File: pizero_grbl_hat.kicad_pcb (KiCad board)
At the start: 2 copper layers, 65 x 30 mm, 31 parts, among them J1 GPIO_CONNECTOR, J2 ISP, J3 LIMIT_X, J4 LIMIT_Y, J5 VMOT, J6 MOTOR_X, J7 MOTOR_Y, U1 ATmega328P-AU, Y1 16MHz

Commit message: finish layout and print schematics
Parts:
- removed A1: X-axis, Module:Pololu_Breakout-16_15.2x20.3mm
- removed C3, C7: 100n, Capacitor_SMD:C_0805_2012Metric
- removed C6: 10u, Capacitor_SMD:C_0805_2012Metric
- removed TP1, TP2, TP3, TP4, TP5, TP6: TestPoint_2Pole, TestPoint:TestPoint_2Pads_Pitch2.54mm_Drill0.8mm
- added C9: 100u, Capacitor_SMD:CP_Elec_6.3x7.7, F.Cu at (153.3, 106.0)
- added I2C: I2C, Connector_JST:JST_PH_B4B-PH-K_1x04_P2.00mm_Vertical, F.Cu at (121.0, 103.0)
- added X-Axis: X-axis, Module:Pololu_Breakout-16_15.2x20.3mm, F.Cu at (140.1, 112.3)
- C1: footprint Capacitor_SMD:C_0805_2012Metric -> Capacitor_SMD:C_0805_2012Metric_Pad1.15x1.40mm_HandSolder; moved to F.Cu
- R1: footprint Resistor_SMD:R_0805_2012Metric -> Resistor_SMD:R_0805_2012Metric_Pad1.15x1.40mm_HandSolder
- Y1: footprint Crystal:Crystal_SMD_2012-2Pin_2.0x1.2mm -> Crystal:Crystal_SMD_Abracon_ABM3-2Pin_5.0x3.2mm_HandSoldering
- moved C2 23.5 mm to (128.6, 98.6)
- moved R2 23.3 mm to (125.0, 98.6)
- moved C8 9.66 mm to (175.9, 105.7), turned to 180 degrees
- moved C1 7.14 mm to (125.1, 107.8), turned to 270 degrees
- moved R1 5.07 mm to (129.7, 108.5), turned to 0 degrees
- moved J2 4.02 mm to (142.6, 103.5), turned to 0 degrees
- moved Y1 2.79 mm to (132.0, 105.2), turned to 0 degrees
- moved C4 2.13 mm to (136.3, 105.2), turned to 270 degrees
- moved U1 1.55 mm to (129.5, 105.2)
- moved C5 1.07 mm to (136.3, 108.8), turned to 270 degrees
- renumbered J3 to Limit-X, J4 to Limit-Y, J6 to Motor-X, J7 to Motor-Y, J5 to VSTEP, A2 to Y-Axis
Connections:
- J1 pad 3: /GPIO2_SDA1 -> SDA
- J1 pad 5: /GPIO3_SCL1 -> SCL
- Y-Axis pad 10: Net-(A2-Pad10) -> +3V3
- Y-Axis pad 11: Net-(A2-Pad11) -> +3V3
- Y-Axis pad 12: Net-(A2-Pad12) -> +3V3
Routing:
- net +3V3: track 142.0 -> 110.7 mm, vias 0 -> 2
- net SCL: track 0.00 -> 15.5 mm
- net SDA: track 0.00 -> 12.4 mm
- net RESET: track 38.9 -> 28.0 mm
- net GND: track 72.2 -> 80.2 mm, vias 7 -> 1
- net Net-(A2-Pad12): track 5.08 -> 0.00 mm
- net Net-(A2-Pad11): track 5.08 -> 0.00 mm
- net Net-(A2-Pad10): track 5.08 -> 0.00 mm
- net Net-(A1-Pad12): track 5.08 -> 0.00 mm
- net Net-(A1-Pad11): track 5.08 -> 0.00 mm
- net Net-(A1-Pad10): track 5.08 -> 0.00 mm
- net MOSI: track 26.1 -> 22.4 mm, vias 2 -> 0
- net STEPX: track 15.2 -> 11.8 mm, vias 1 -> 0
- net DIRX: track 20.9 -> 17.5 mm
- net Net-(A1-Pad8): track 47.0 -> 44.0 mm
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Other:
- board text added: "GRBL-Hat rev0"
- board text added: "daniel@tydirium.org"
- board text removed: "GRBL Hat rev0 (c) 2019 Daniel Winters daniel@tydirium.org"

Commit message: start working on rev1, work in progress
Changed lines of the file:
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@@
-(kicad_pcb (version 20171130) (host pcbnew "(5.1.4-0-10_14)")
+(kicad_pcb (version 20171130) (host pcbnew "(5.1.5-0-10_14)")
   (general
     (thickness 1.6)
@@
   )
   (layers
-    (0 F.Cu signal)
+    (0 F.Cu signal hide)
     (31 B.Cu signal)
-    (32 B.Adhes user)
-    (33 F.Adhes user)
+    (32 B.Adhes user hide)
+    (33 F.Adhes user hide)
     (34 B.Paste user)
-    (35 F.Paste user)
+    (35 F.Paste user hide)
     (36 B.SilkS user)
-    (37 F.SilkS user)
+    (37 F.SilkS user hide)
     (38 B.Mask user)
     (39 F.Mask user)
@@
     (descr "Pololu Breakout 16-pin 15.2x20.3mm 0.6x0.8\\")
     (tags "Pololu Breakout")
-    (fp_text reference X-Axis (at 6.35 -2.54 90) (layer F.SilkS)
+    (fp_text reference X-Axis (at 6.35 -2.032 90) (layer F.SilkS)
       (effects (font (size 1 1) (thickness 0.15)))
     )
@@
     (descr "Through hole straight socket strip, 2x20, 2.54mm pitch, double cols (from Kicad 4.0.7), script generated")
     (tags "Through hole socket strip THT 2x20 2.54mm double row")
-    (fp_text reference J1 (at 2.8 -16.3) (layer B.SilkS)
+    (fp_text reference J1 (at 1.778 -20.53) (layer B.SilkS)
       (effects (font (size 1 1) (thickness 0.15)) (justify mirror))
     )
@@
     (tags capacitor)
     (attr smd)
-    (fp_text reference C2 (at 0 1.65) (layer B.SilkS)
+    (fp_text reference C2 (at -2.8725 0.508) (layer B.SilkS)
       (effects (font (size 1 1) (thickness 0.15)) (justify mirror))
     )
@@
     (tags capacitor)
     (attr smd)
-    (fp_text reference C4 (at 0 1.65 90) (layer B.SilkS)
+    (fp_text reference C4 (at -0.1755 -1.778 90) (layer B.SilkS)
       (effects (font (size 1 1) (thickness 0.15)) (justify mirror))
     )
@@
     (tags capacitor)
     (attr smd)
-    (fp_text reference C5 (at 0 1.65 270) (layer B.SilkS)
+    (fp_text reference C5 (at -0.508 -1.778 270) (layer B.SilkS)
       (effects (font (size 1 1) (thickness 0.15)) (justify mirror))
     )
@@
     (tags "QFP 0.8")
     (attr smd)
-    (fp_text reference U1 (at 0 6.05 180) (layer B.SilkS)
+    (fp_text reference U1 (at -4.699 5.061 180) (layer B.SilkS)
       (effects (font (size 1 1) (thickness 0.15)) (justify mirror))
     )
@@
     (tags "resistor handsolder")
     (attr smd)
-    (fp_text reference R1 (at 0 1.524) (layer F.SilkS)
+    (fp_text reference R1 (at 0 2.032) (layer F.SilkS)
       (effects (font (size 1 1) (thickness 0.15)))
     )
@@
     )
   )
-  (gr_text daniel@tydirium.org (at 130.938 101.172) (layer F.SilkS)
+  (gr_text daniel@tydirium.org (at 131.192 100.664) (layer F.SilkS)
     (effects (font (size 1 1) (thickness 0.15)))
   )
-  (gr_text "GRBL-Hat rev0" (at 129.668 98.378) (layer F.SilkS)
+  (gr_text "GRBL-Hat rev0" (at 129.414 99.14) (layer F.SilkS)
     (effects (font (size 1 1) (thickness 0.15)))
   )

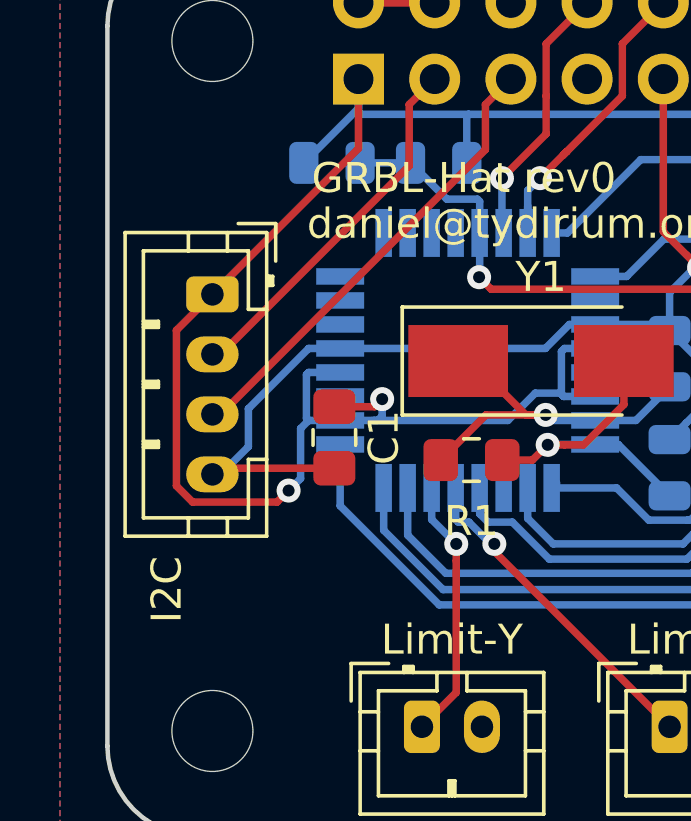
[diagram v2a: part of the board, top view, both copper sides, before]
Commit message: show I2C pins on front and back silkscreen
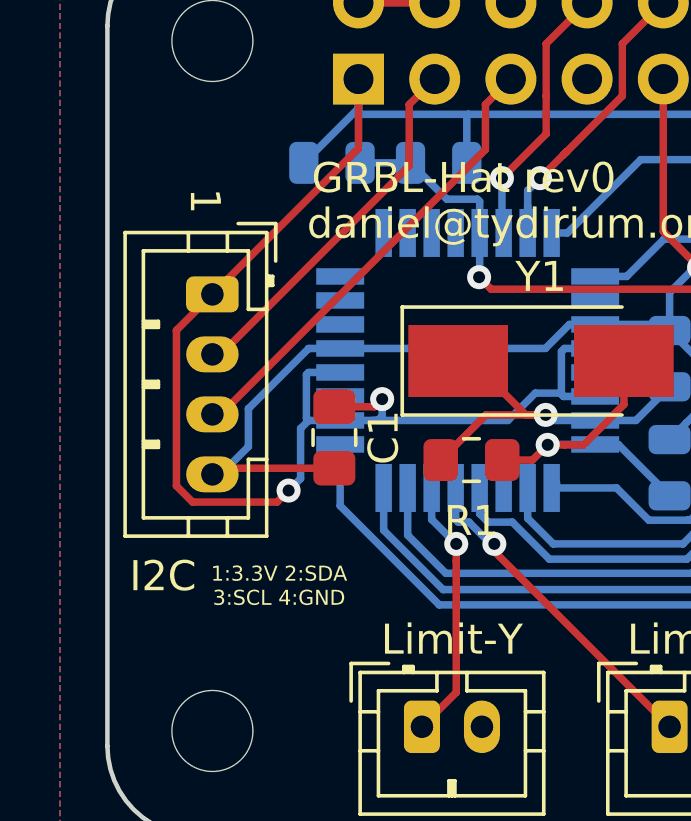
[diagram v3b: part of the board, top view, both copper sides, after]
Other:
- board text added: "1"
- board text added: "1:3.3V 2:SDA 3:SCL 4:GND"
- board text added: "3.3V"
- board text added: "GND"
- board text added: "SCL"
- board text added: "SDA"
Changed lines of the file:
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@@
   (general
     (thickness 1.6)
-    (drawings 22)
+    (drawings 28)
     (tracks 308)
     (zones 0)
@@
   )
   (layers
-    (0 F.Cu signal hide)
+    (0 F.Cu signal)
     (31 B.Cu signal)
     (32 B.Adhes user hide)
-    (33 F.Adhes user hide)
+    (33 F.Adhes user)
     (34 B.Paste user)
     (35 F.Paste user hide)
     (36 B.SilkS user)
-    (37 F.SilkS user hide)
+    (37 F.SilkS user)
     (38 B.Mask user)
     (39 F.Mask user)
@@
     (descr "JST PH series connector, B4B-PH-K (http://www.jst-mfg.com/product/pdf/eng/ePH.pdf), generated with kicad-footprint-generator")
     (tags "connector JST PH side entry")
-    (fp_text reference I2C (at 9.842 1.524 90) (layer F.SilkS)
+    (fp_text reference I2C (at 9.3975 1.651 180) (layer F.SilkS)
       (effects (font (size 1 1) (thickness 0.15)))
     )
@@
     )
   )
+  (gr_text "1:3.3V 2:SDA\n3:SCL 4:GND" (at 123.2545 112.729) (layer F.SilkS)
+    (effects (font (size 0.5 0.5) (thickness 0.125)))
+  )
+  (gr_text 1 (at 120.778 99.902 -90) (layer F.SilkS)
+    (effects (font (size 1 1) (thickness 0.15)))
+  )
+  (gr_text SCL (at 118.873 107.141 -90) (layer B.SilkS)
+    (effects (font (size 0.7 0.7) (thickness 0.15)) (justify mirror))
+  )
+  (gr_text SDA (at 118.873 104.9185 -90) (layer B.SilkS)
+    (effects (font (size 0.7 0.7) (thickness 0.15)) (justify mirror))
+  )
+  (gr_text GND (at 118.873 109.6175 -90) (layer B.SilkS)
+    (effects (font (size 0.7 0.7) (thickness 0.15)) (justify mirror))
+  )
+  (gr_text 3.3V (at 118.873 102.3785 -90) (layer B.SilkS)
+    (effects (font (size 0.7 0.7) (thickness 0.15)) (justify mirror))
+  )
   (gr_text daniel@tydirium.org (at 131.192 100.664) (layer F.SilkS)
